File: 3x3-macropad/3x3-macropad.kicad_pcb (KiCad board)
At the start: 2 copper layers, 38 parts, among them SW1 SW_Push, SW2 RotaryEncoder_Switch, U1 ATmega32U4-A, Y1 16MHz

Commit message: first attempt routing 3x3
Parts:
- moved F1 9.51 mm to (150.6, 49.8)
- moved R2 9.51 mm to (155.4, 49.2)
- moved USB1 9.51 mm to (154.6, 39.6)
- moved R1 9.51 mm to (153.0, 49.2)
- moved SW1 9.28 mm to (163.0, 42.1)
- moved R5 7.31 mm to (248.9, 59.5)
- moved R6 2.24 mm to (242.6, 59.5)
- moved C6 1.59 mm to (154.4, 66.6), turned to 90 degrees
- moved R7 1.59 mm to (246.5, 59.5)
- moved R3 1.12 mm to (158.6, 49.2)
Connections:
- U1 pad 22: unconnected-(U1-PD5-Pad22) -> ROW2
- U1 pad 25: unconnected-(U1-PD4-Pad25) -> ROW1
- U1 pad 26: unconnected-(U1-PD6-Pad26) -> ROW0
- U1 pad 27: unconnected-(U1-PD7-Pad27) -> COL2
- U1 pad 28: unconnected-(U1-PB4-Pad28) -> COL1
- U1 pad 29: unconnected-(U1-PB5-Pad29) -> COL0
- U1 pad 30: unconnected-(U1-PB6-Pad30) -> ENCA
- U1 pad 31: unconnected-(U1-PC6-Pad31) -> ENCB
- U1 pad 32: unconnected-(U1-PC7-Pad32) -> ENCBTN
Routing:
- net +5V: track 0.00 -> 227.6 mm, vias 0 -> 5
- net COL0: track 0.00 -> 224.0 mm
- net COL1: track 0.00 -> 203.5 mm
- net COL2: track 0.00 -> 182.5 mm
- net ROW0: track 0.00 -> 165.1 mm
- net ROW1: track 0.00 -> 144.9 mm
- net ENCBTN: track 0.00 -> 144.6 mm
- net ENCB: track 0.00 -> 125.6 mm
- net ENCA: track 0.00 -> 123.9 mm
- net GND: track 9.76 -> 124.3 mm
- net ROW2: track 0.00 -> 93.0 mm, vias 0 -> 2
- net Net-(U1-D-): track 0.00 -> 23.9 mm
- net Net-(U1-D+): track 0.00 -> 23.2 mm
- net Net-(U1-~{RESET}): track 0.00 -> 22.1 mm
- net unconnected-(USB1-SHIELD-Pad6): track 0.00 -> 16.3 mm
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- added copper zone on B.Cu, net GND
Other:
- board outline added: 108.6 x 58.7 mm

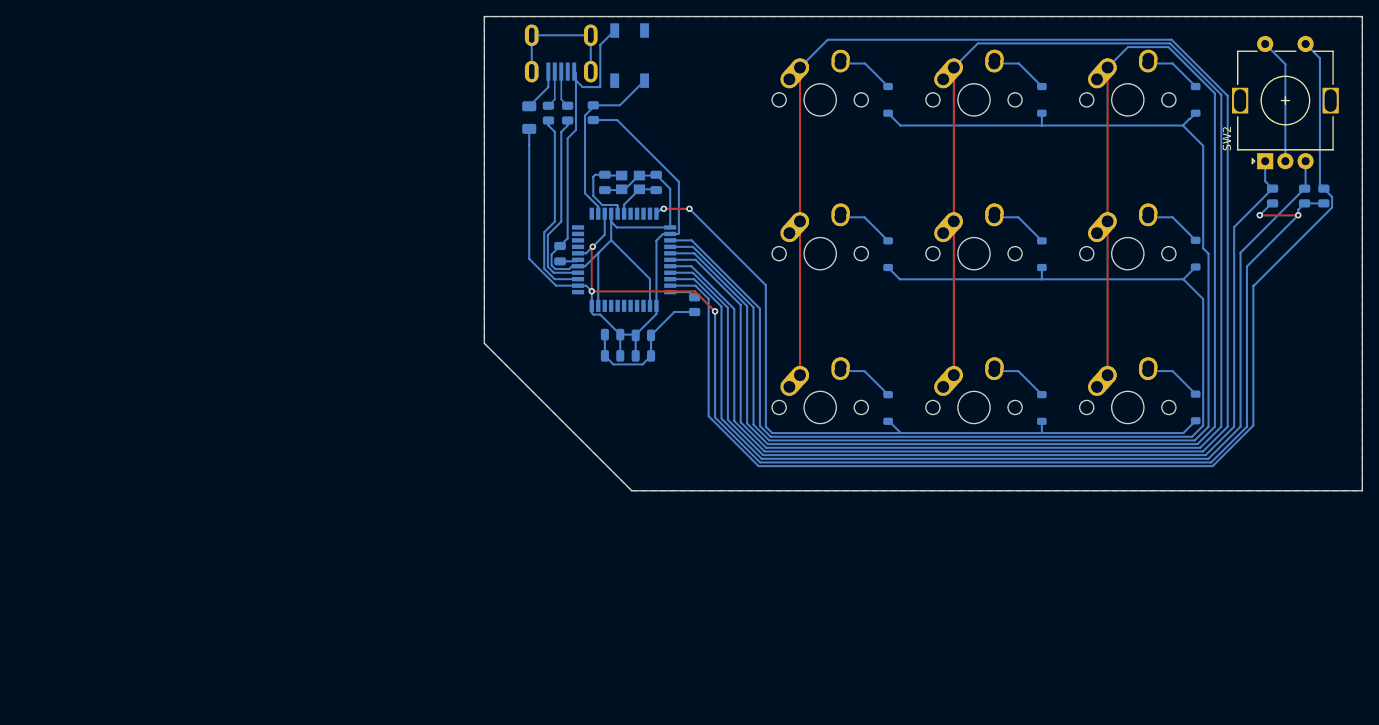
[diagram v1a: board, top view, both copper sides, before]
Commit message: redo pcb routing (better)
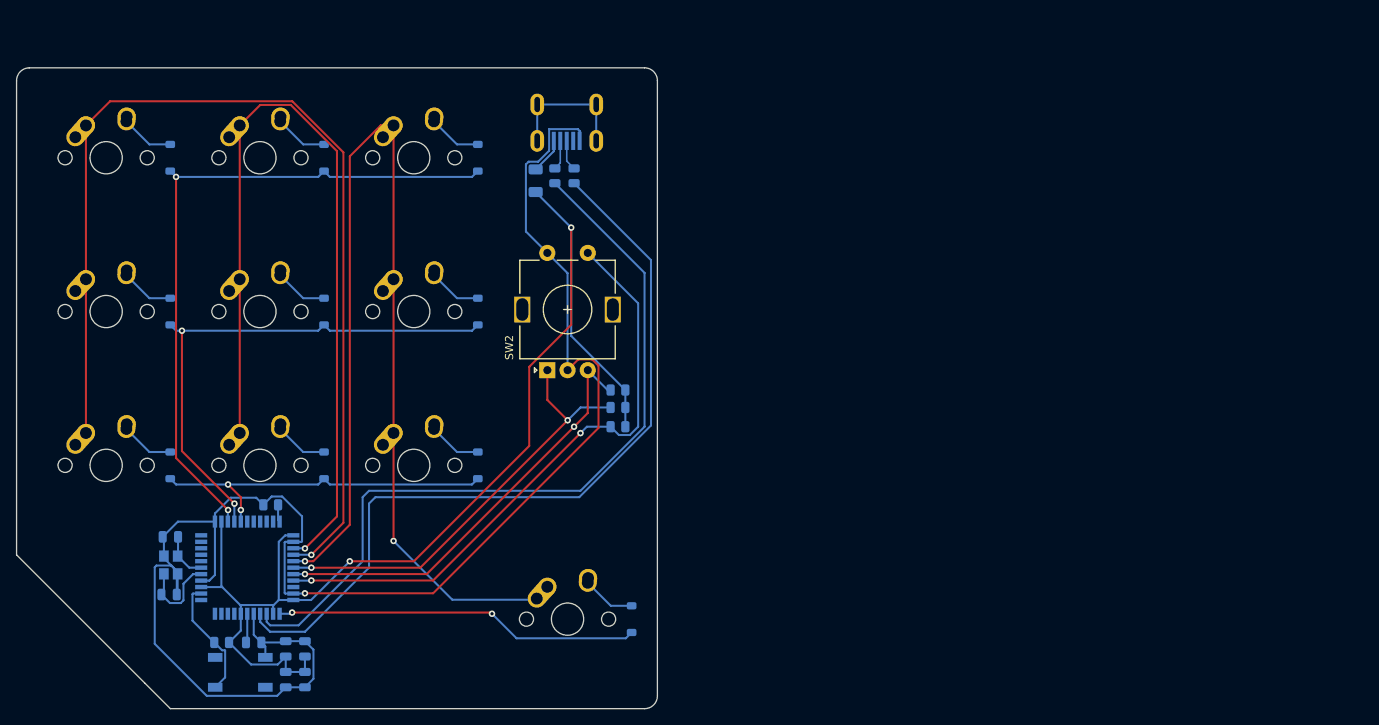
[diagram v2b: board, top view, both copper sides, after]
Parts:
- added D10: SOD_123, Diode_SMD:D_SOD-123, B.Cu at (163.3, 111.8)
- added MX10: MX-NoLED, MX_Alps_Hybrid:MX-1U-NoLED, F.Cu at (155.4, 111.8)
- moved SW2 92.5 mm to (152.9, 81.0)
- moved R5 91.9 mm to (161.6, 88.0), turned to 180 degrees
- moved SW1 90.2 mm to (114.9, 118.4), turned to 0 degrees
- moved D1 89.1 mm to (106.2, 54.7)
- moved D3 89.1 mm to (144.3, 54.7)
- moved D6 89.1 mm to (144.3, 73.7)
- moved D9 89.1 mm to (144.3, 92.8)
- moved D2 89.1 mm to (125.2, 54.7)
- moved D4 89.1 mm to (106.2, 73.7)
- moved D7 89.1 mm to (106.2, 92.8)
- moved D5 89.1 mm to (125.2, 73.7)
- moved D8 89.1 mm to (125.2, 92.8)
- moved MX4 88.6 mm to (98.3, 73.7)
- moved MX6 88.6 mm to (136.3, 73.7)
- moved MX1 88.6 mm to (98.3, 54.7)
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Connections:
- U1 pad 1: unconnected-(U1-PE6-Pad1) -> ROW3
- U1 pad 22: ROW2 -> unconnected-(U1-PD5-Pad22)
- U1 pad 25: ROW1 -> ROW0
- U1 pad 26: ROW0 -> ROW1
- U1 pad 27: COL2 -> ROW2
- U1 pad 28: COL1 -> unconnected-(U1-PB4-Pad28)
- U1 pad 29: COL0 -> unconnected-(U1-PB5-Pad29)
- U1 pad 30: ENCA -> unconnected-(U1-PB6-Pad30)
- U1 pad 31: ENCB -> unconnected-(U1-PC6-Pad31)
- U1 pad 32: ENCBTN -> unconnected-(U1-PC7-Pad32)
- U1 pad 36: unconnected-(U1-PF7-Pad36) -> COL1
- U1 pad 37: unconnected-(U1-PF6-Pad37) -> COL0
- U1 pad 38: unconnected-(U1-PF5-Pad38) -> COL2
- U1 pad 39: unconnected-(U1-PF4-Pad39) -> ENCA
- U1 pad 40: unconnected-(U1-PF1-Pad40) -> ENCB
- U1 pad 41: unconnected-(U1-PF0-Pad41) -> ENCBTN
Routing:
- net COL1: track 203.5 -> 111.7 mm, vias 0 -> 1
- net COL0: track 224.0 -> 133.4 mm, vias 0 -> 1
- net ROW0: track 165.1 -> 84.6 mm, vias 0 -> 2
- net ROW1: track 144.9 -> 65.6 mm, vias 0 -> 2
- net GND: track 124.3 -> 203.6 mm, vias 0 -> 1
- net +5V: track 227.6 -> 150.9 mm, vias 5 -> 2
- net Net-(U1-D+): track 23.2 -> 99.0 mm
- net Net-(U1-D-): track 23.9 -> 97.5 mm
- net ENCB: track 125.6 -> 53.8 mm, vias 0 -> 2
- net ENCA: track 123.9 -> 54.7 mm, vias 0 -> 2
- net ENCBTN: track 144.6 -> 75.5 mm, vias 0 -> 2
- net ROW2: track 93.0 -> 44.5 mm
- net ROW3: track 0.00 -> 45.2 mm, vias 0 -> 2
- net COL2: track 182.5 -> 143.6 mm, vias 0 -> 2
- net Net-(U1-~{RESET}): track 22.1 -> 15.0 mm
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- removed copper zone on B.Cu, net GND
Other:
- board size 108.6 x 58.7 mm -> 79.3 x 79.3 mm
